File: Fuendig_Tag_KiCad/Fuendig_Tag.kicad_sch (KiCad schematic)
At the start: 3 parts, among them U1 STM32C011J4Mx

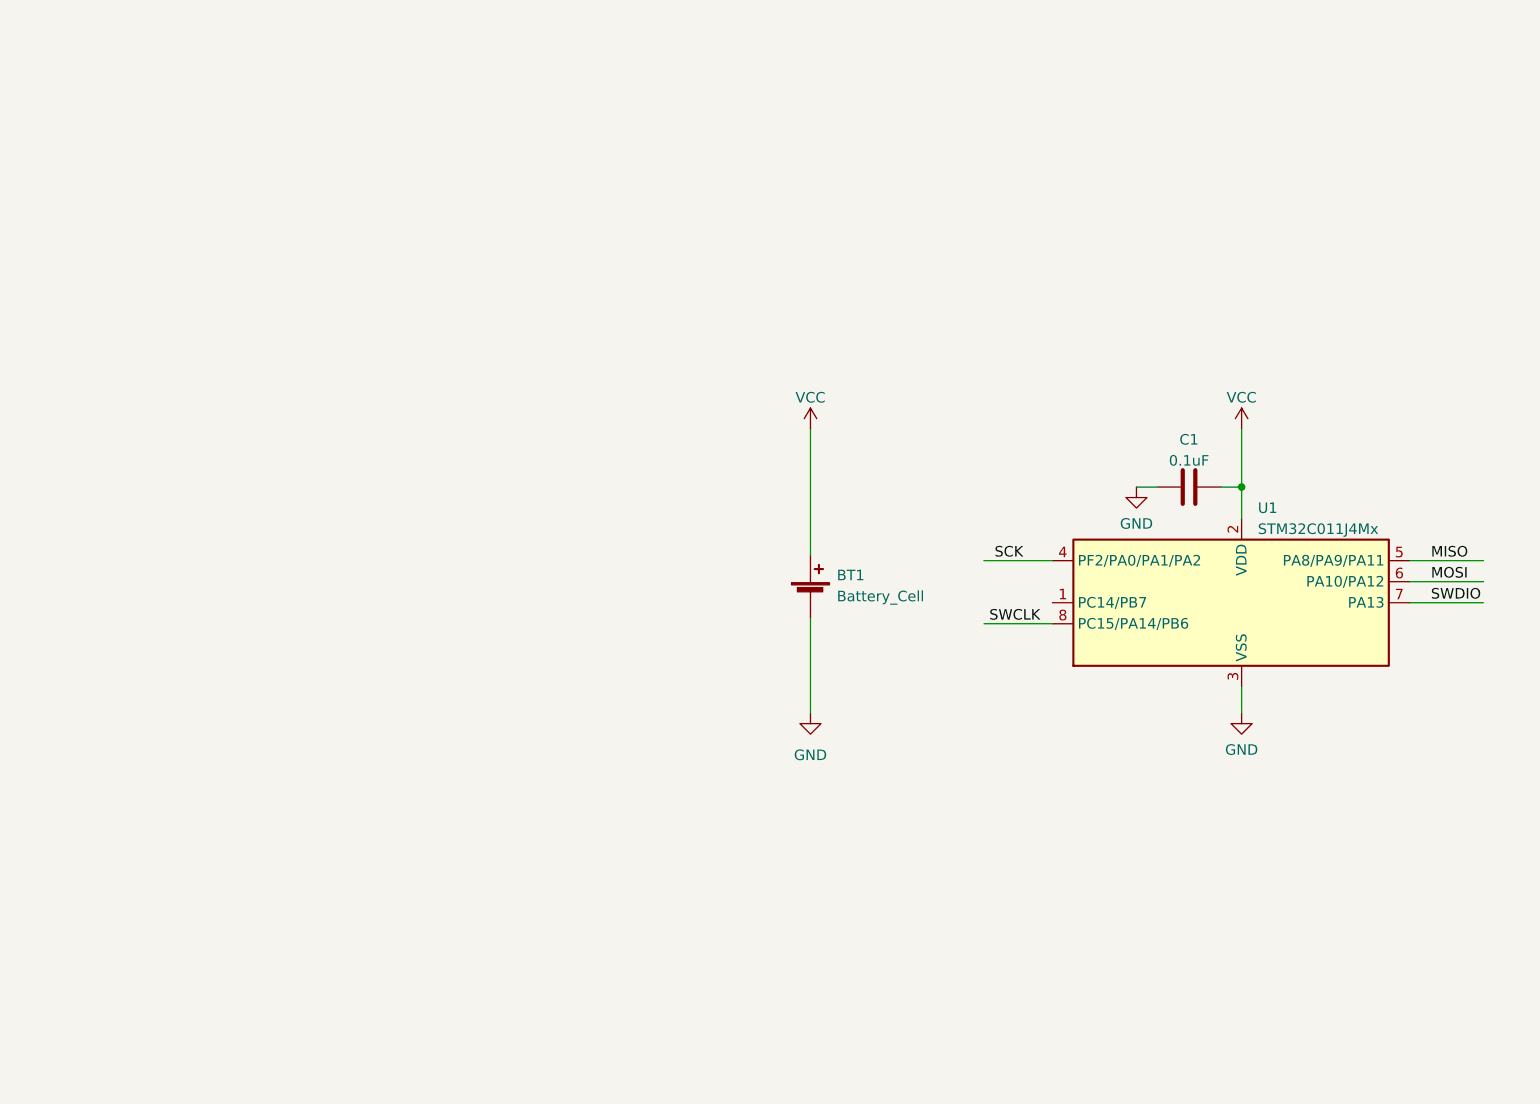
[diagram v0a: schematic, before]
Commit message: Parts preselected, MCU connections drafted.
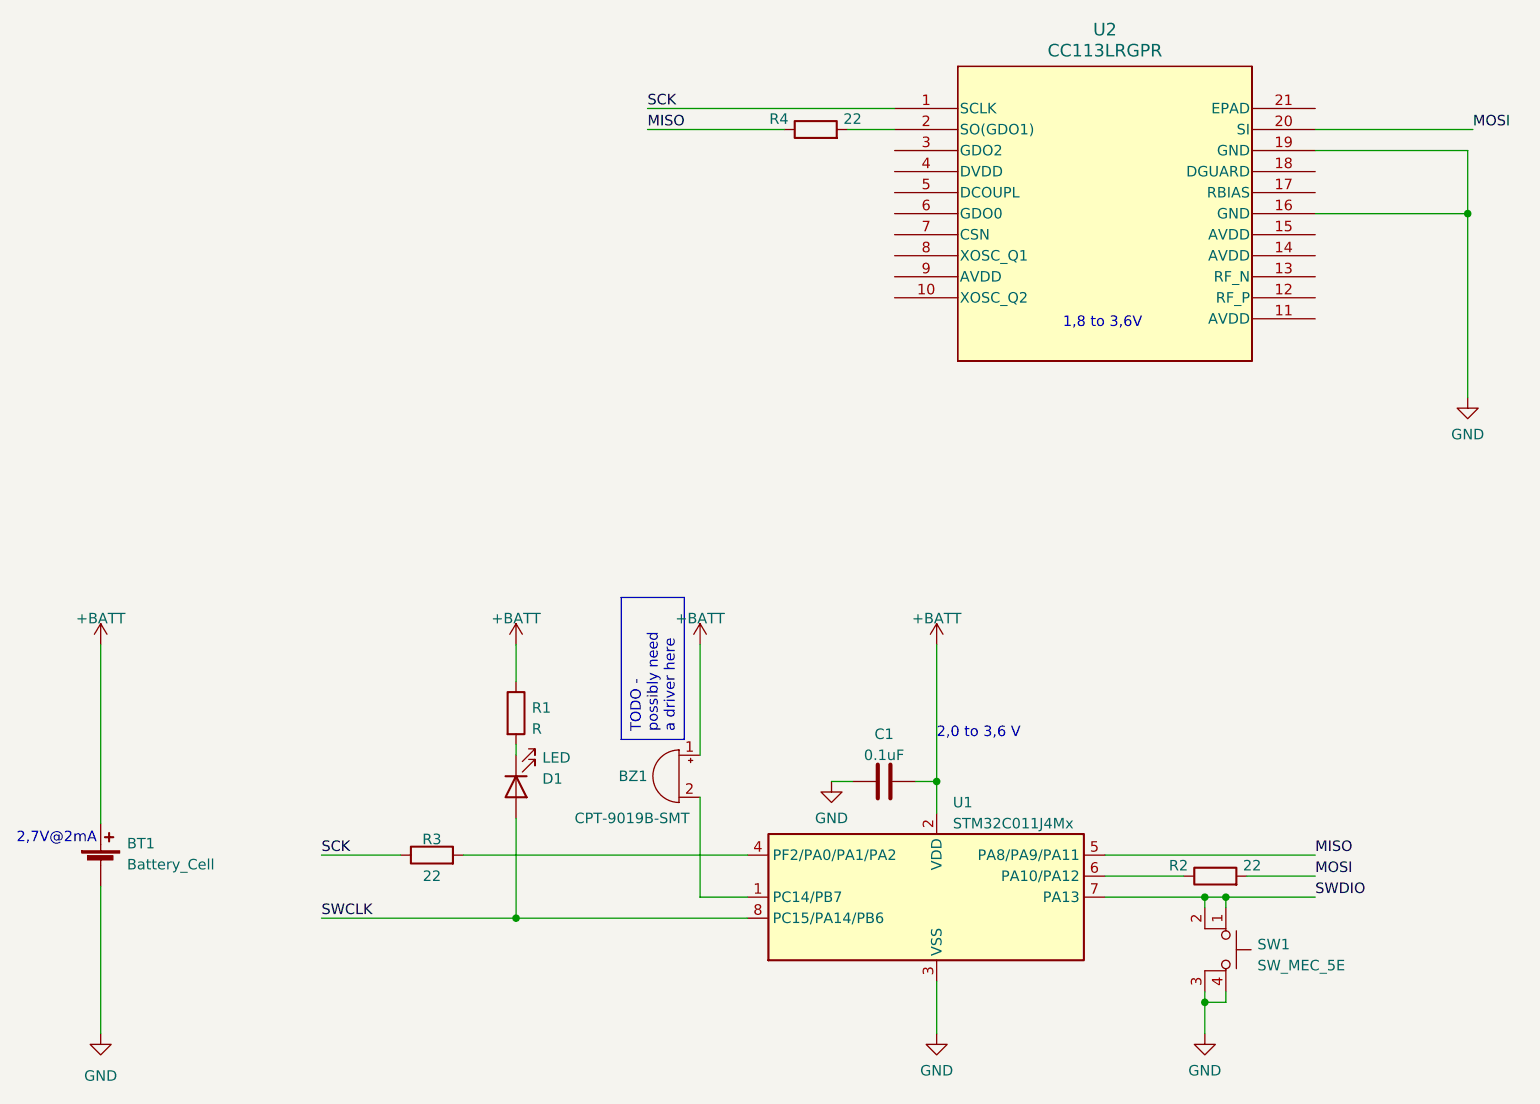
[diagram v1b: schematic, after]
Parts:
- added BZ1: CPT-9019B-SMT, Buzzer_Beeper:Buzzer_CUI_CPT-9019S-SMT, symbol Device:Buzzer
- added D1: LED, LED_SMD:LED_2010_5025Metric, symbol Device:LED
- added R1: R, symbol Device:R
- added R2, R3, R4: 22, symbol Device:R
- added SW1: SW_MEC_5E, Button_Switch_SMD:SW_MEC_5GSH9, symbol Switch:SW_MEC_5E
- added U2: CC113LRGPR, RGP20_2P4X2P4_TEX, symbol Fuendig_symbols:CC113LRGPR
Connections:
- net GND: now also SW1.3 (K), SW1.4 (A), U2.16 (GND), U2.19 (GND)
- net MISO: now also R4.1
- net MOSI: now also R2.2, U2.20 (SI); no longer U1.6 (PA10/PA12)
- net SCK: now also R3.1, U2.1 (SCLK); no longer U1.4 (PF2/PA0/PA1/PA2)
- net SWCLK: now also D1.2 (A)
- net SWDIO: now also SW1.1, SW1.2
- net at U1.1 (PC14/PB7): now also BZ1.2 (+)
- net VCC renamed +BATT
- net +BATT: now also BZ1.1 (-), R1.1
- new net: R3.2, U1.4 (PF2/PA0/PA1/PA2)
- new net: R2.1, U1.6 (PA10/PA12)
- new net: D1.1 (K), R1.2
- new net: R4.2, U2.2 (SO(GDO1))
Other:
- note added: "1,8 to 3,6V"
- note added: "2,0 to 3,6 V"
- note added: "2,7V@2mA"
- moved on the sheet: BT1, C1, U1
